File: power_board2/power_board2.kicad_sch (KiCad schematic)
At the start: 24 parts, among them IC1 ADP3338AKCZ-5-REEL, U1 NUCLEO-F303K8

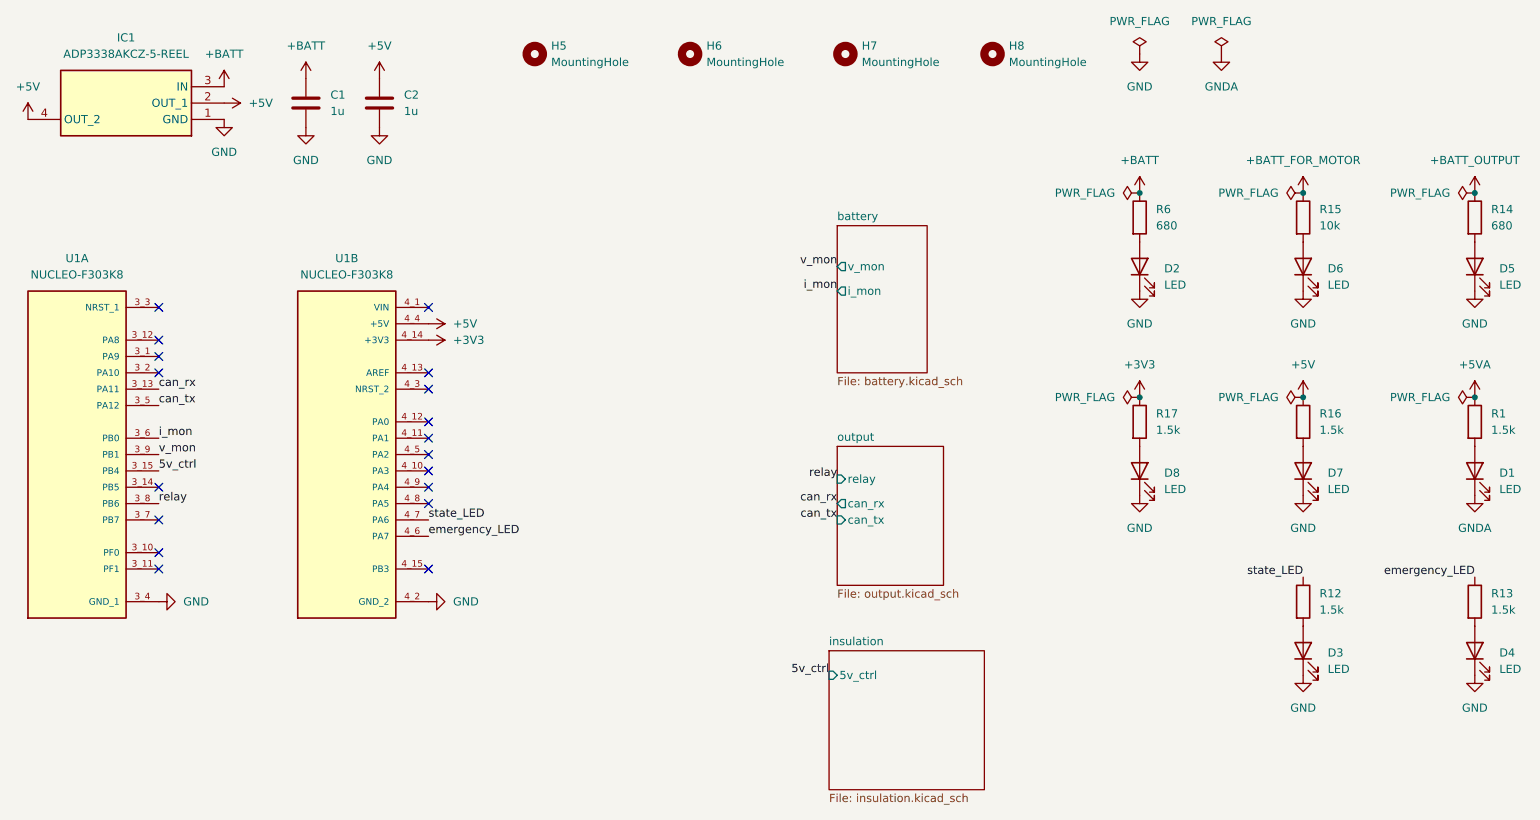
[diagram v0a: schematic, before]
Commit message: 非常停止スイッチを追加
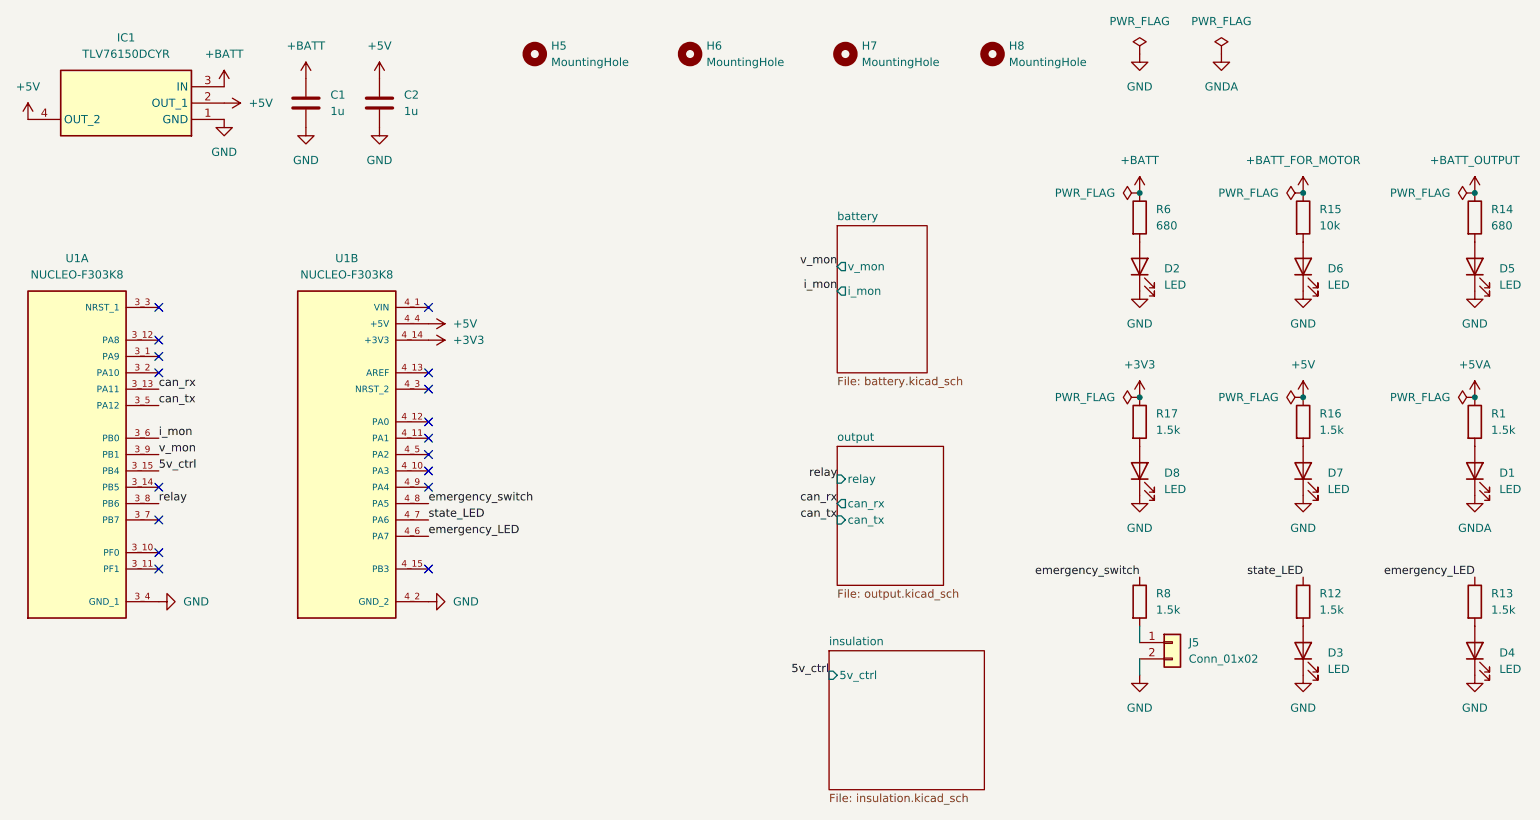
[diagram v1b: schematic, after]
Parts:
- removed IC1: ADP3338AKCZ-5-REEL, power_board2:SOT230P700X180-4N, symbol power_board2:ADP3338AKCZ-5-REEL
- added IC1: TLV76150DCYR, SOT230P700X180-4N, symbol power_board2:TLV76150DCYR
- added J5: Conn_01x02, Connector_JST:JST_VH_B2P-VH_1x02_P3.96mm_Vertical, symbol Connector_Generic:Conn_01x02
- added R8: 1.5k, Resistor_SMD:R_0603_1608Metric, symbol Device:R
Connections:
- net +5V: now also IC1.2 (OUT_1), IC1.4 (OUT_2)
- net +BATT: now also IC1.3 (IN)
- net GND: now also IC1.1 (GND), J5.2 (Pin_2)
- net emergency_switch: now reaches U1.4_8 (PA5)
- net emergency_switch: now also R8.1
- new net: J5.1 (Pin_1), R8.2
- no-connect marks 18 -> 17
